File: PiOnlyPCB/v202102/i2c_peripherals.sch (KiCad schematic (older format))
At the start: 28 parts, among them J4 Conn_01x04, J5 Conn_01x04, J6 Conn_01x04, J7 Conn_01x04, J8 Conn_01x08, J9 Conn_01x08, U2 PCF8574, U3 PCF8574

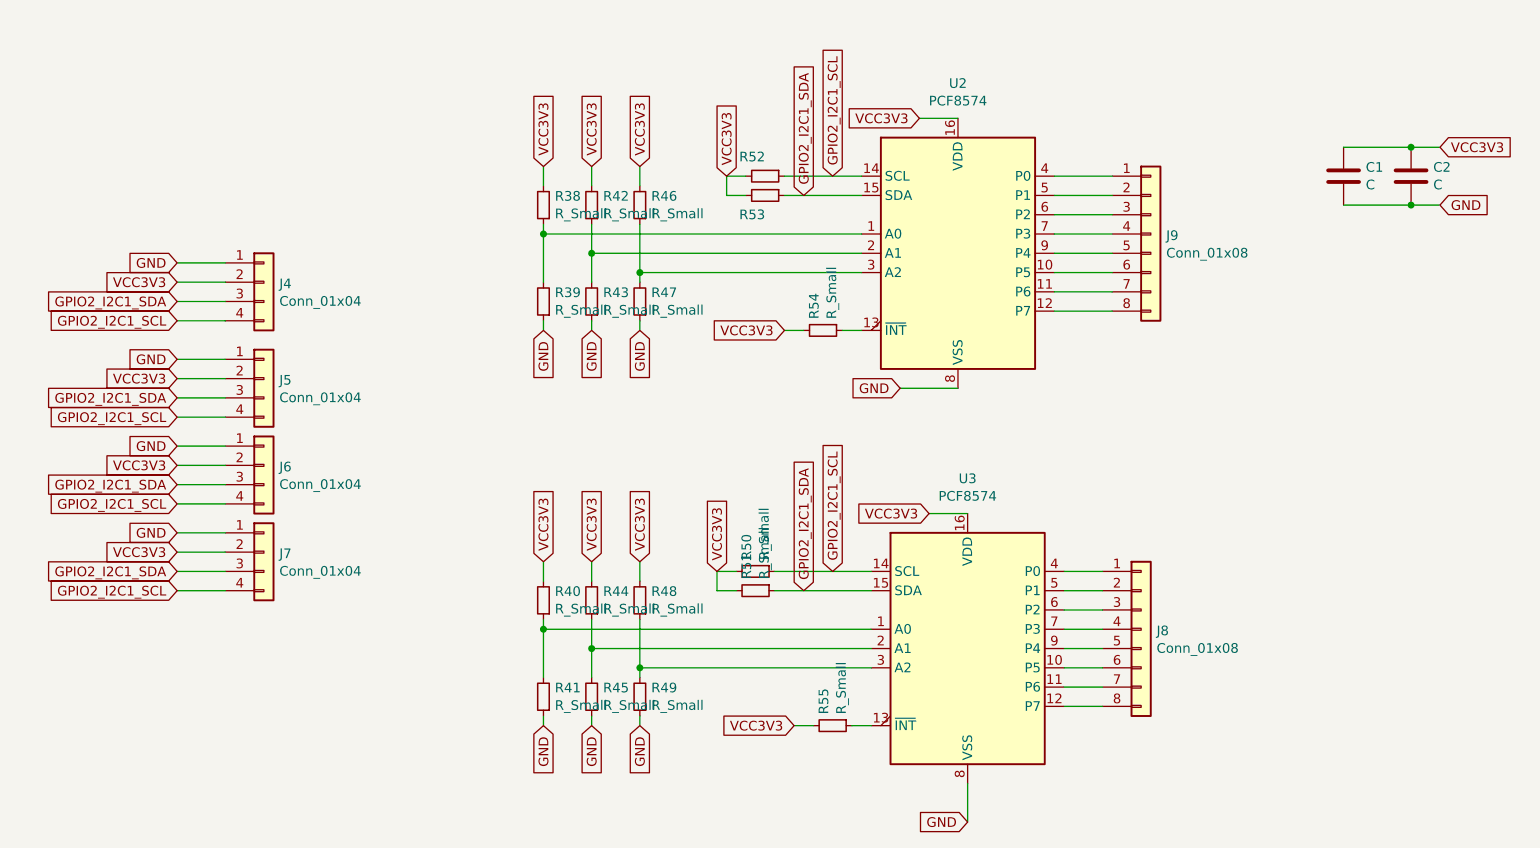
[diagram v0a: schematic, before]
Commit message: PiOnlyPCB 202102: Routed again without I2C expanders, before IN* nets routed.
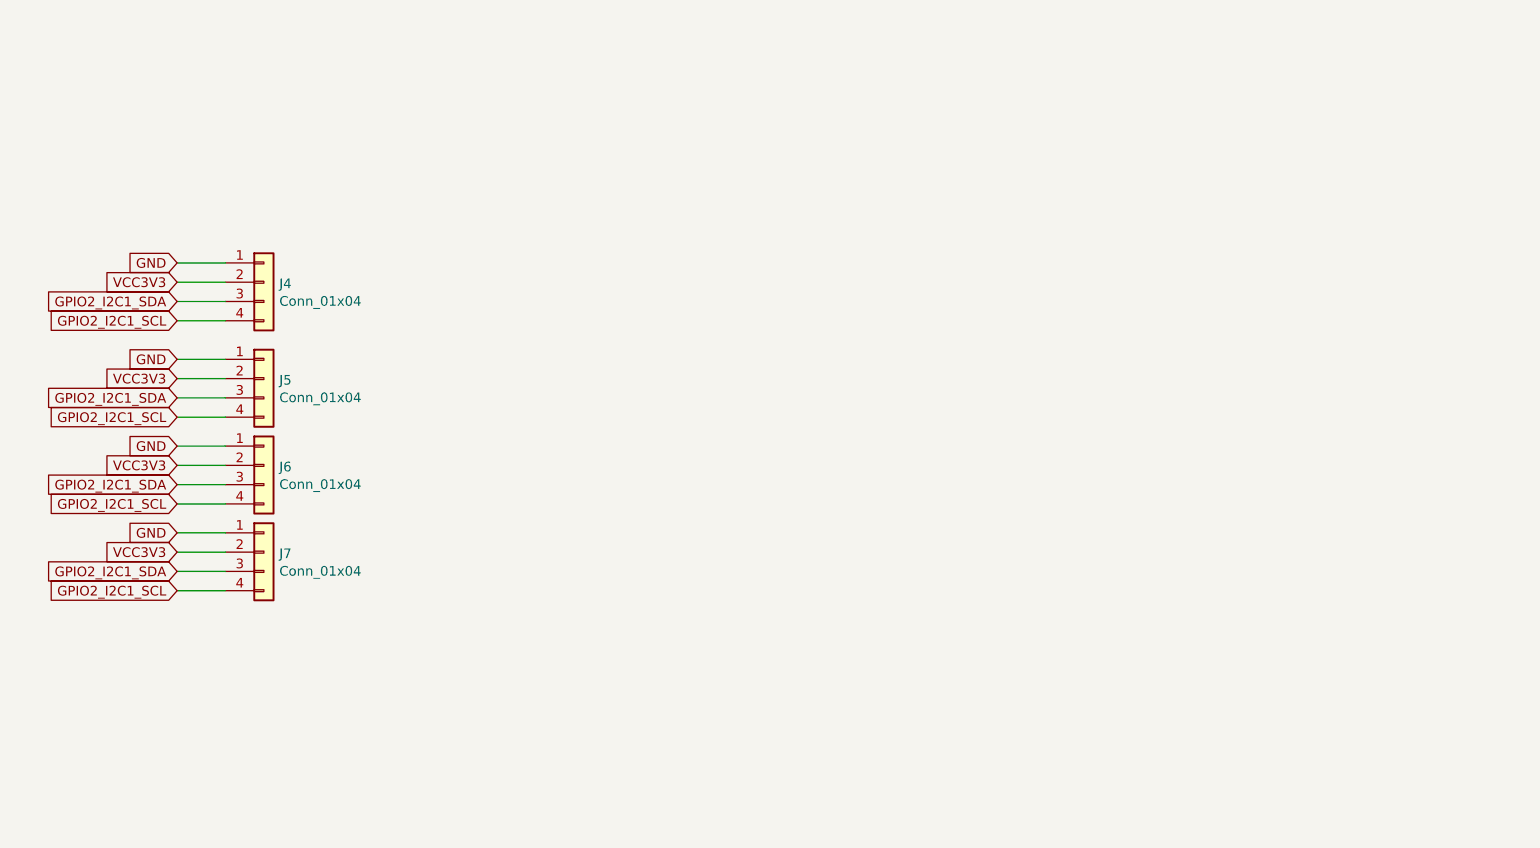
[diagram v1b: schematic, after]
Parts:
- removed C1, C2: C, Capacitor_SMD:C_0805_2012Metric_Pad1.18x1.45mm_HandSolder, symbol Device:C
- removed J8, J9: Conn_01x08, Connector_PinHeader_2.54mm:PinHeader_1x08_P2.54mm_Vertical, symbol Connector_Generic:Conn_01x08
- removed R38, R39, R40, R41, R42, R43, R44, R45, R46, R47, R48, R49, R50, R51, R52, R53, R54, R55: R_Small, Resistor_SMD:R_0805_2012Metric_Pad1.20x1.40mm_HandSolder, symbol Device:R_Small
- removed U2, U3: PCF8574, Package_SO:SOIC-16W_7.5x10.3mm_P1.27mm, symbol Interface_Expansion:PCF8574
